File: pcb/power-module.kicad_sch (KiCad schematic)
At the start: 37 parts, among them J1 USB_C_PowerOnly_6P, J2 Power, U1 AZ1084-3.3, U2 LM66200DRLR

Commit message: Updated resistor values
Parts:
- R4: value 1k -> 4.7k; Digikey 541-1.00KHTR-ND -> 541-3993-2-ND; LCSC C2907113 -> C2907166; MN Vishay -> FOJAN; MPN CRCW06031K00FKEA -> FRC0603J472 TS; Mouser 71-CRCW0603-1.0K-E3 -> 71-CRCW06034K70JNEAC
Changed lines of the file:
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@@
 	)
 	(symbol
+		(lib_id "Device:R_Small")
+		(at 163.83 177.8 0)
+		(unit 1)
+		(exclude_from_sim no)
+		(in_bom yes)
+		(on_board yes)
+		(dnp no)
+		(property "Reference" "R4"
+			(at 165.3286 176.6316 0)
+			(effects
+				(font
+					(size 1 1)
+				)
+				(justify left)
+			)
+		)
+		(property "Value" "4.7k"
+			(at 165.3286 178.943 0)
+			(effects
+				(font
+					(size 1 1)
+				)
+				(justify left)
+			)
+		)
+		(property "Footprint" "Resistor_SMD:R_0603_1608Metric"
+			(at 163.83 177.8 0)
+			(effects
+				(font
+					(size 1 1)
+					(color 223 129 255 1)
+				)
+				(hide yes)
+			)
+		)
+		(property "Datasheet" "https://www.vishay.com/docs/28773/crcwce3.pdf"
+			(at 163.83 177.8 0)
+			(effects
+				(font
+					(size 1 1)
+					(color 223 129 255 1)
+				)
+				(hide yes)
+			)
+		)
+		(property "Description" "Thick Film Resistors - SMD 1/10Watt 4.7Kohms 5% Commercial Use"
+			(at 163.83 177.8 0)
+			(effects
+				(font
+					(size 1.27 1.27)
+				)
+				(hide yes)
+			)
+		)
+		(property "MN" "FOJAN"
+			(at 163.83 177.8 0)
+			(effects
+				(font
+					(size 1.27 1.27)
+				)
+				(hide yes)
+			)
+		)
+		(property "MPN" "FRC0603J472 TS"
+			(at 163.83 177.8 0)
+			(effects
+				(font
+					(size 1.27 1.27)
+				)
+				(hide yes)
+			)
+		)
+		(property "Mouser" "71-CRCW06034K70JNEAC"
+			(at 163.83 177.8 0)
+			(effects
+				(font
+					(size 1 1)
+					(color 223 129 255 1)
+				)
+				(hide yes)
+			)
+		)
+		(property "Digikey" "541-3993-2-ND"
+			(at 163.83 177.8 0)
+			(effects
+				(font
+					(size 1 1)
+					(color 223 129 255 1)
+				)
+				(hide yes)
+			)
+		)
+		(property "LCSC" "C2907166"
+			(at 163.83 177.8 0)
+			(effects
+				(font
+					(size 1 1)
+					(color 223 129 255 1)
+				)
+				(hide yes)
+			)
+		)
+		(pin "1"
+		)
+		(pin "2"
+		)
+		(instances
+			(project "power-module"
+				(path "/445c1fff-2e1a-48b1-a91f-a137832edebf"
+					(reference "R4")
+					(unit 1)
+				)
+			)
+		)
+	)
+	(symbol
 		(lib_id "Mechanical:MountingHole")
 		(at 30.48 187.96 0)
@@
 					(unit 1)
 				)
-			)
-		)
-	)
-	(symbol
-		(lib_id "Device:R_Small")
-		(at 163.83 177.8 0)
-		(unit 1)
-		(exclude_from_sim no)
-		(in_bom yes)
-		(on_board yes)
-		(dnp no)
-		(property "Reference" "R4"
-			(at 165.3286 176.6316 0)
-			(effects
-				(font
-					(size 1 1)
-				)
-				(justify left)
-			)
-		)
-		(property "Value" "1k"
-			(at 165.3286 178.943 0)
-			(effects
-				(font
-					(size 1 1)
-				)
-				(justify left)
-			)
-		)
-		(property "Footprint" "Resistor_SMD:R_0603_1608Metric"
-			(at 163.83 177.8 0)
-			(effects
-				(font
-					(size 1 1)
-					(color 223 129 255 1)
-				)
-				(hide yes)
-			)
-		)
-		(property "Datasheet" "https://www.vishay.com/docs/20035/dcrcwe3.pdf"
-			(at 163.83 177.8 0)
-			(effects
-				(font
-					(size 1 1)
-					(color 223 129 255 1)
-				)
-				(hide yes)
-			)
-		)
-		(property "Description" "Thick Film Resistors - SMD 1/10watt 1.0Kohms 1%"
-			(at 163.83 177.8 0)
-			(effects
-				(font
-					(size 1.27 1.27)
-				)
-				(hide yes)
-			)
-		)
-		(property "MN" "Vishay"
-			(at 163.83 177.8 0)
-			(effects
-				(font
-					(size 1.27 1.27)
-				)
-				(hide yes)
-			)
-		)
-		(property "MPN" "CRCW06031K00FKEA"
-			(at 163.83 177.8 0)
-			(effects
-				(font
-					(size 1.27 1.27)
-				)
-				(hide yes)
-			)
-		)
-		(property "Mouser" "71-CRCW0603-1.0K-E3"
-			(at 163.83 177.8 0)
-			(effects
-				(font
-					(size 1 1)
-					(color 223 129 255 1)
-				)
-				(hide yes)
-			)
-		)
-		(property "Digikey" "541-1.00KHTR-ND"
-			(at 163.83 177.8 0)
-			(effects
-				(font
-					(size 1 1)
-					(color 223 129 255 1)
-				)
-				(hide yes)
-			)
-		)
-		(property "LCSC" "C2907113"
-			(at 163.83 177.8 0)
-			(effects
-				(font
-					(size 1 1)
-					(color 223 129 255 1)
-				)
-				(hide yes)
-			)
-		)
-		(pin "1"
-		)
-		(pin "2"
-		)
-		(instances
-			(project "power-module"
-				(path "/445c1fff-2e1a-48b1-a91f-a137832edebf"
-					(reference "R4")
-					(unit 1)
-				)

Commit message: Minor clean up and dimensioning
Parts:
- J2: symbol CRGM Connector:JST-SH-4 -> CRGM Connector:AQ_POWER; MPN SM04B-SRSS-TB -> SM04B-SRSS-TBT(LF)(SN); Mouser 306-SM04BSRSSTBLFSN -> 306-SM04BSRSSTBTLFSN
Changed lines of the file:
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@@
 	)
 	(symbol
-		(lib_id "CRGM Connector:JST-SH-4")
+		(lib_id "CRGM Connector:AQ_POWER")
 		(at 99.06 116.84 0)
 		(unit 1)
@@
 		)
 		(property "Footprint" "CRGM Connector:JST_SH_SM04B-SRSS-TB_1x04-1MP_P1.00mm_Horizontal"
-			(at 102.616 107.95 0)
+			(at 102.108 130.556 0)
 			(effects
 				(font
@@
 		)
 		(property "Datasheet" "https://www.jst-mfg.com/product/pdf/eng/eSH.pdf"
-			(at 99.06 116.84 0)
+			(at 102.616 144.272 0)
 			(effects
 				(font
@@
 			)
 		)
-		(property "Description" "JST SH 1.0mm 4 Position"
-			(at 102.87 110.236 0)
+		(property "Description" "4 Position, 1mm pitch"
+			(at 102.108 132.842 0)
 			(effects
 				(font
@@
 		)
 		(property "MN" "JST"
-			(at 99.06 116.84 0)
+			(at 102.362 128.524 0)
 			(effects
 				(font
@@
 			)
 		)
-		(property "MPN" "SM04B-SRSS-TB"
-			(at 99.06 116.84 0)
+		(property "MPN" "SM04B-SRSS-TBT(LF)(SN)"
+			(at 102.87 135.382 0)
 			(effects
 				(font
@@
 			)
 		)
-		(property "Mouser" "306-SM04BSRSSTBLFSN"
-			(at 99.06 116.84 0)
+		(property "Mouser" "306-SM04BSRSSTBTLFSN"
+			(at 102.616 137.922 0)
 			(effects
 				(font
@@
 		)
 		(property "Digikey" "455-SM04B-SRSS-TBTR-ND"
-			(at 99.06 116.84 0)
+			(at 102.616 140.208 0)
 			(effects
 				(font
@@
 		)
 		(property "LCSC" "C2763614"
-			(at 99.06 116.84 0)
+			(at 102.108 142.24 0)
 			(effects
 				(font

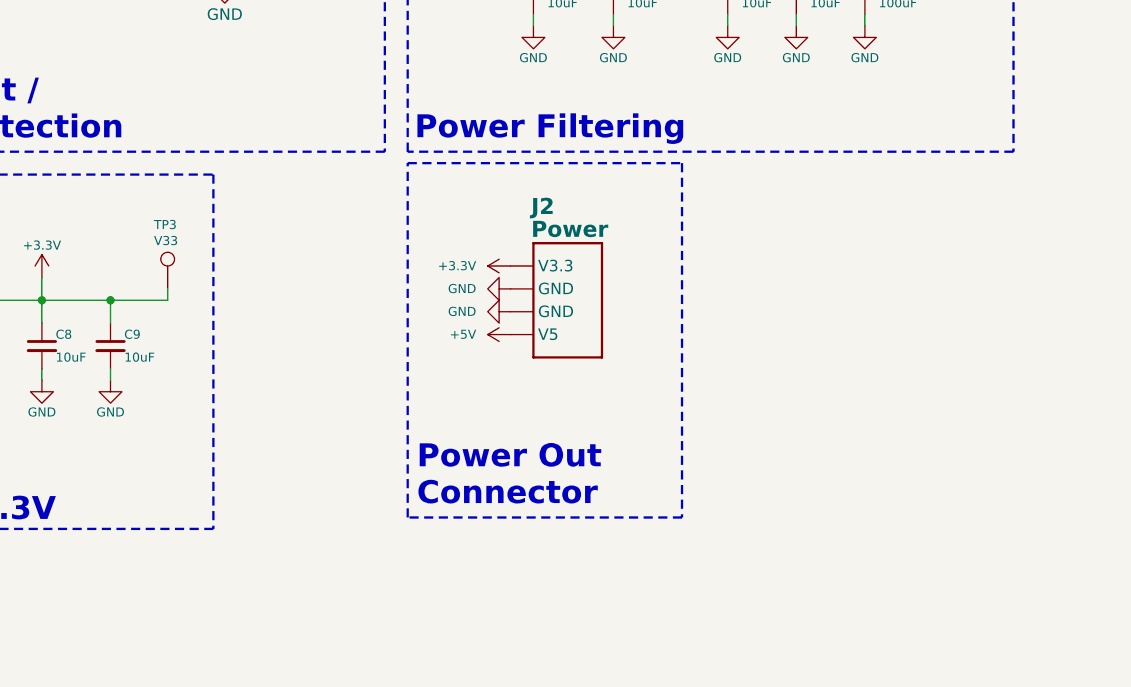
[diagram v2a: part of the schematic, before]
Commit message: Added second power connector and TP for GND
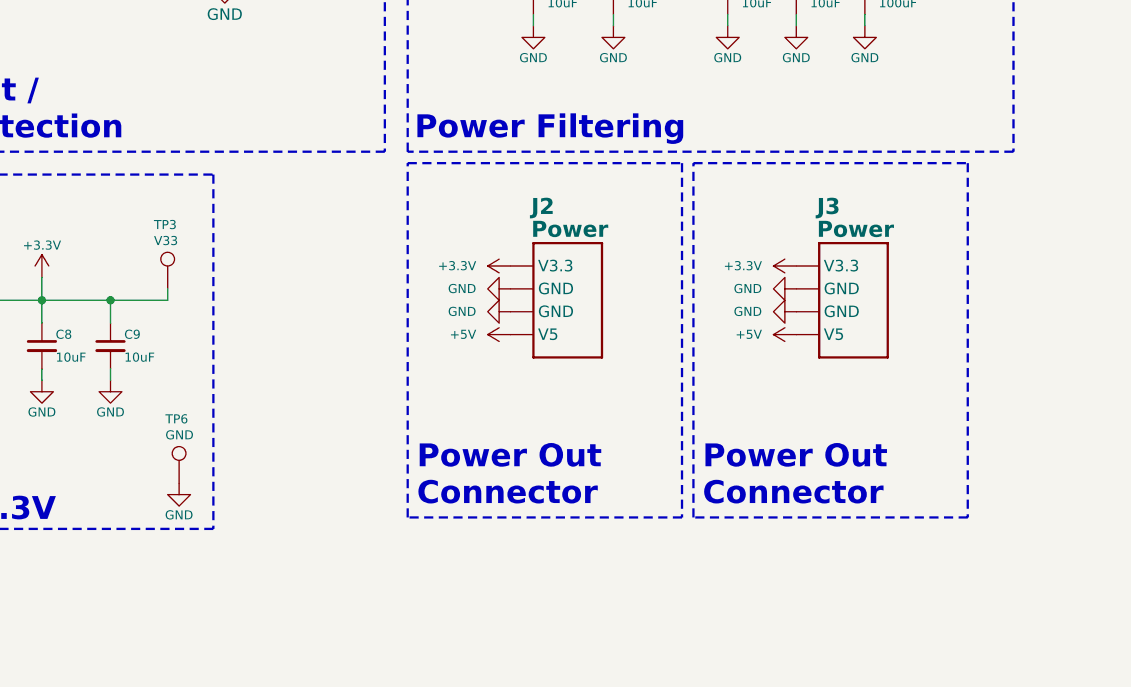
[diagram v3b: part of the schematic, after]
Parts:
- added J3: Power, CRGM Connector:JST_SH_SM04B-SRSS-TB_1x04-1MP_P1.00mm_Horizontal, symbol CRGM Connector:AQ_POWER
- added TP6: GND, CRGM Mechanical:TestPoint_Pad_D1.0mm, symbol Connector:TestPoint
- TP1, TP2, TP3, TP4, TP5: footprint TestPoint:TestPoint_Pad_D1.0mm -> CRGM Mechanical:TestPoint_Pad_D1.0mm
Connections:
- net +3.3V: now also J3.4 (V3.3)
- net +5V: now also J3.1 (V5)
- net GND: now also J3.2 (GND), J3.3 (GND), TP6.1
